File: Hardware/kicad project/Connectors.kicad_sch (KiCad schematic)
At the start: 21 parts, among them IC5 USBLC6-2SC6, J1 SWD header, J2 216990-0003, J3 MEM2061-01-188-00-A, Q1 BSS316NH6327XTSA1

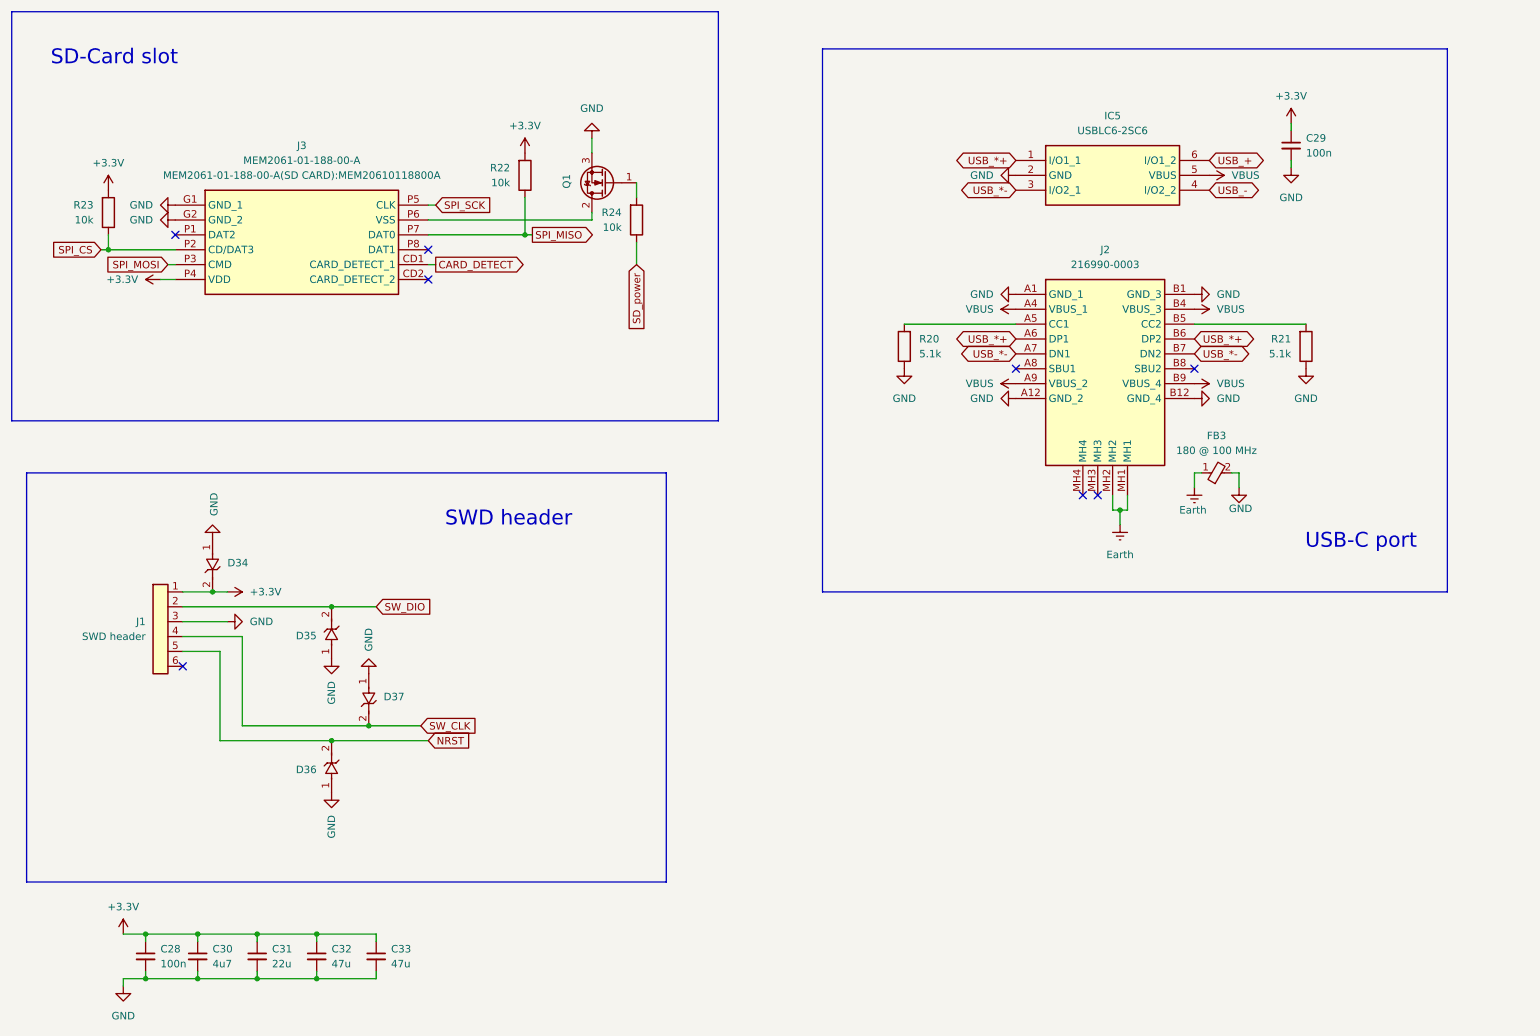
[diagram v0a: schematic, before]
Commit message: added notes to mistake on PCB
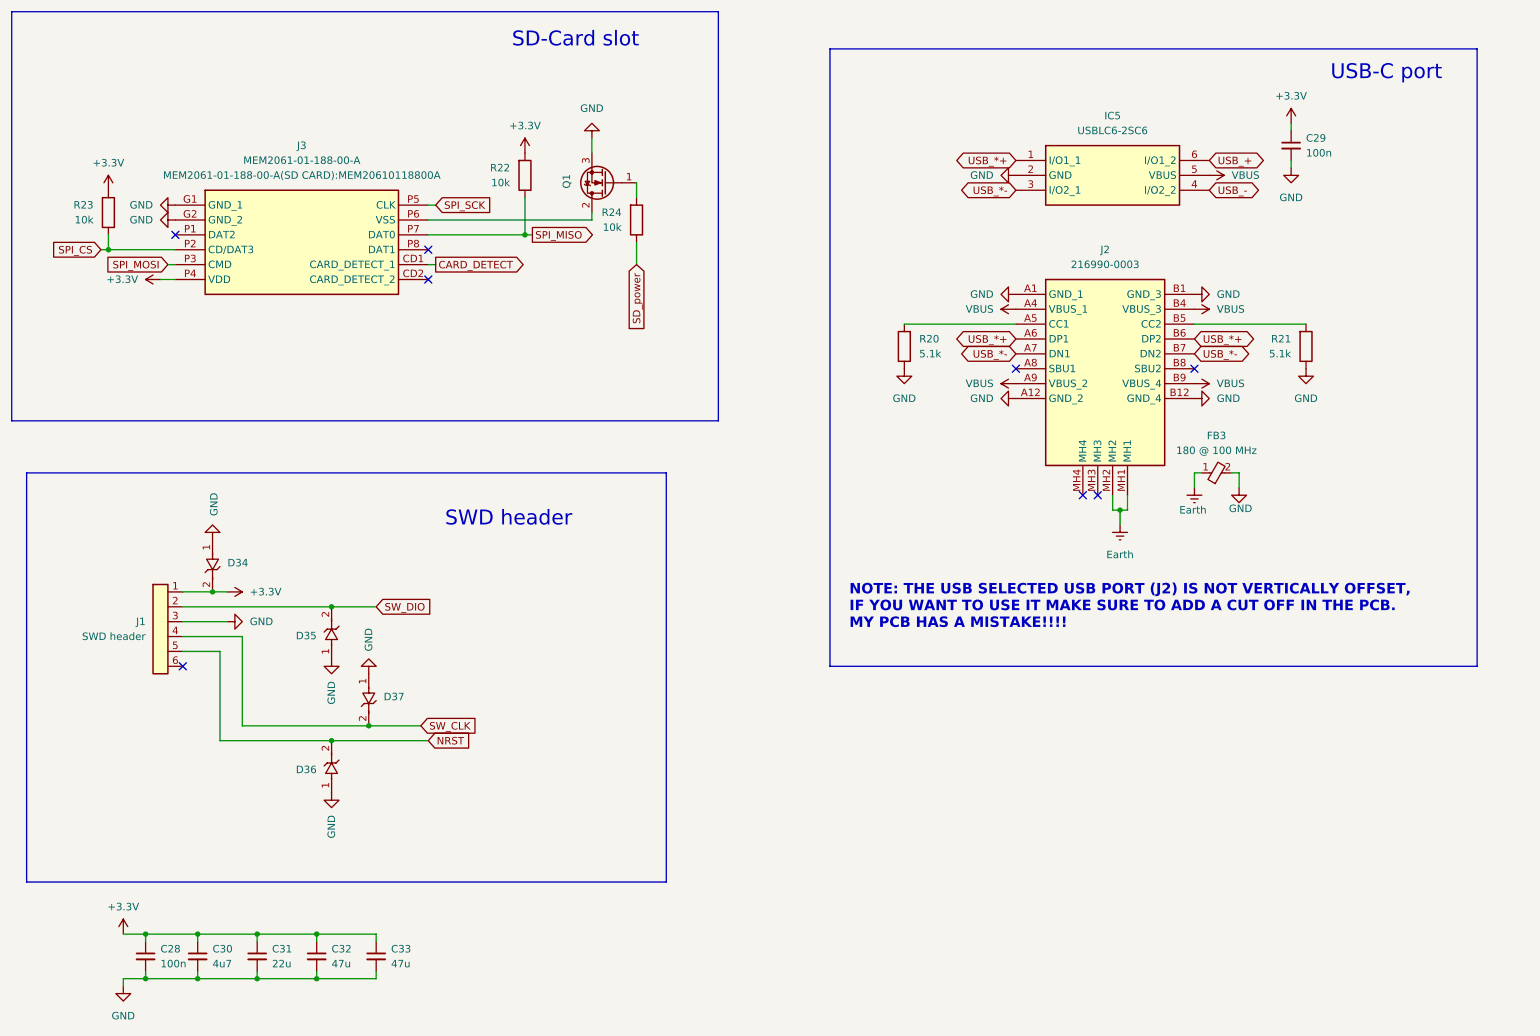
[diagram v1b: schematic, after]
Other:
- note added: "NOTE: THE USB SELECTED USB PORT (J2) IS NOT VERTICALLY OFFSET, IF YOU WANT TO USE IT MAKE SURE TO ADD A CUT OFF IN THE PCB. MY PCB HAS A MISTAKE!!!!"
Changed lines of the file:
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@@
 	)
 	(rectangle
-		(start 158.75 26.67)
-		(end 265.43 119.38)
+		(start 160.02 26.67)
+		(end 270.51 132.08)
 		(stroke
 			(width 0)
@@
 	(text "USB-C port"
 		(exclude_from_sim no)
-		(at 250.698 110.744 0)
+		(at 255.016 30.734 0)
 		(effects
 			(font
 				(size 2.54 2.54)
 			)
+		)
+	)
+	(text "NOTE: THE USB SELECTED USB PORT (J2) IS NOT VERTICALLY OFFSET, \nIF YOU WANT TO USE IT MAKE SURE TO ADD A CUT OFF IN THE PCB.\nMY PCB HAS A MISTAKE!!!!\n"
+		(exclude_from_sim no)
+		(at 163.322 121.92 0)
+		(effects
+			(font
+				(size 1.778 1.778)
+				(thickness 0.254)
+				(bold yes)
+				(color 255 11 57 1)
+			)
+			(justify left)
 		)
 	)
@@
 	(text "SD-Card slot"
 		(exclude_from_sim no)
-		(at 37.846 28.194 0)
+		(at 116.586 25.146 0)
 		(effects
 			(font

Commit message: Added small comments to the problems of the schematic, SD card.
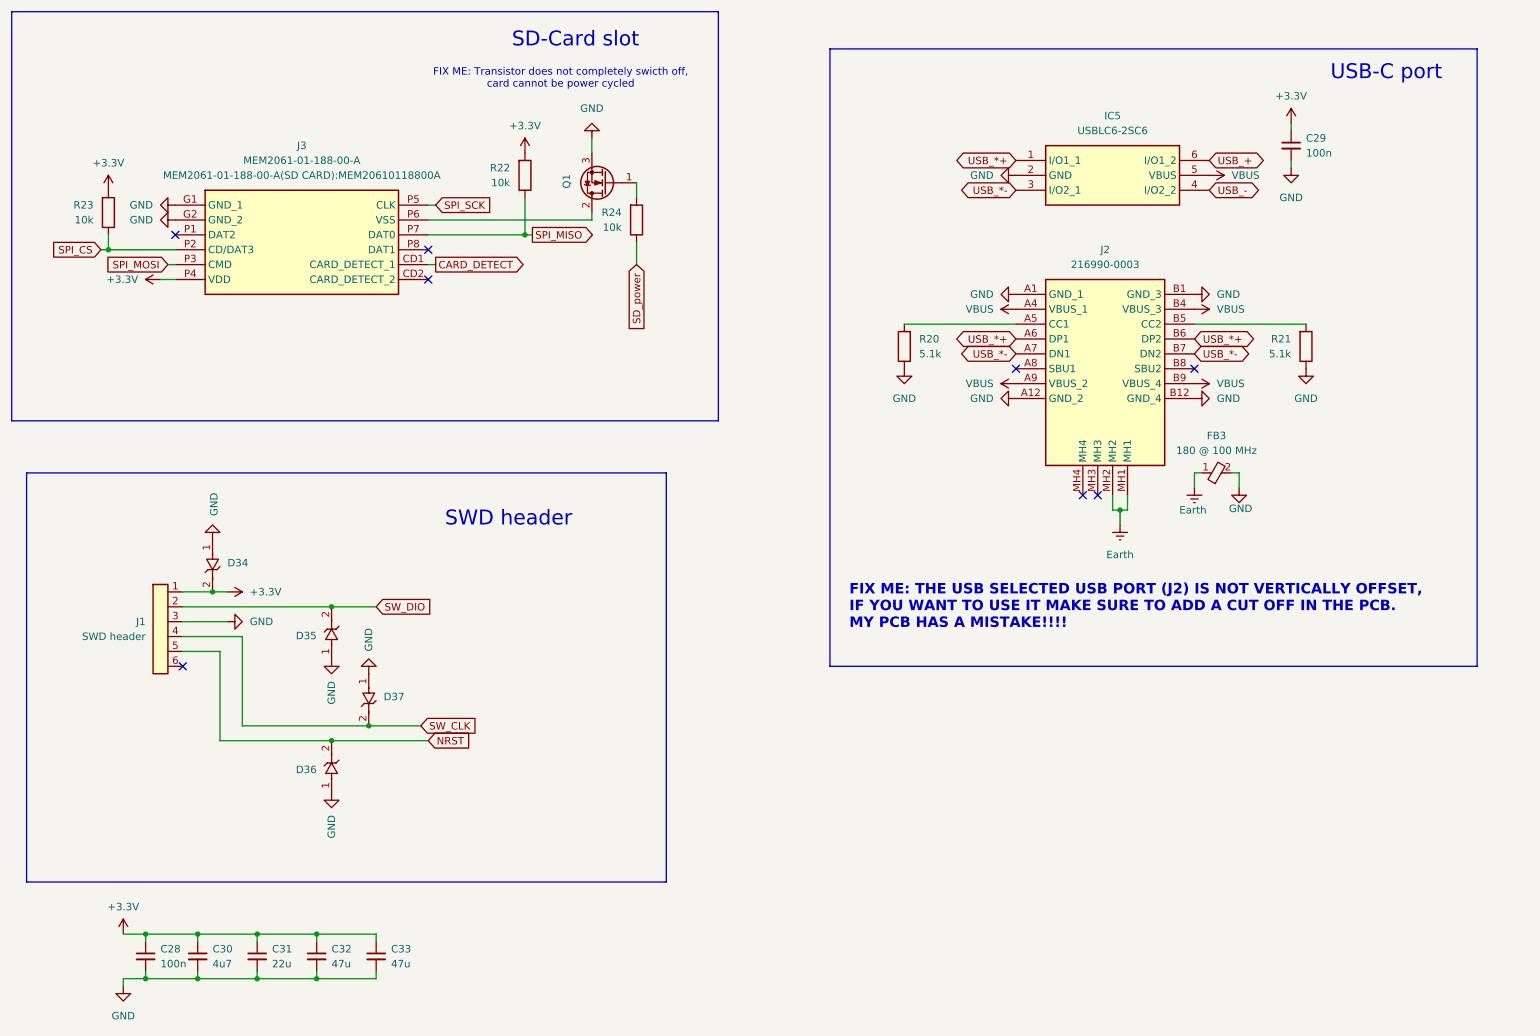
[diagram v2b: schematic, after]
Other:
- note added: "FIX ME: THE USB SELECTED USB PORT (J2) IS NOT VERTICALLY OFFSET, IF YOU WANT TO USE IT MAKE SURE TO ADD A CUT OFF IN THE PCB. MY PCB HAS A MISTAKE!!!!"
- note added: "FIX ME: Transistor does not completely swicth off, card cannot be power cycled"
- note removed: "NOTE: THE USB SELECTED USB PORT (J2) IS NOT VERTICALLY OFFSET, IF YOU WANT TO USE IT MAKE SURE TO ADD A CUT OFF IN THE PCB. MY PCB HAS A MISTAKE!!!!"
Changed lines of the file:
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@@
 		)
 	)
-	(text "NOTE: THE USB SELECTED USB PORT (J2) IS NOT VERTICALLY OFFSET, \nIF YOU WANT TO USE IT MAKE SURE TO ADD A CUT OFF IN THE PCB.\nMY PCB HAS A MISTAKE!!!!\n"
+	(text "FIX ME: THE USB SELECTED USB PORT (J2) IS NOT VERTICALLY OFFSET, \nIF YOU WANT TO USE IT MAKE SURE TO ADD A CUT OFF IN THE PCB.\nMY PCB HAS A MISTAKE!!!!\n"
 		(exclude_from_sim no)
 		(at 163.322 121.92 0)
@@
 			)
 		)
+	)
+	(text "FIX ME: Transistor does not completely swicth off, \ncard cannot be power cycled"
+		(exclude_from_sim no)
+		(at 114.046 31.75 0)
+		(effects
+			(font
+				(size 1.27 1.27)
+			)
+		)
